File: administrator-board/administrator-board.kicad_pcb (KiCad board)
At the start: 2 copper layers, 24 parts, among them J2 Conn_01x06, J3 Conn_01x06, SW2 SW_Push, SW3 SW_Push, SW4 SW_Push, SW5 SW_Push

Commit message: 基盤PCB途中までいけた
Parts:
- moved REF** 3.91 mm to (154.0, 94.0)
- moved REF** 2.50 mm to (154.0, 129.0)
- moved R5 2.26 mm to (135.5, 111.8)
- moved REF** 2.00 mm to (87.0, 129.0)
- moved D5 1.88 mm to (135.5, 107.0)
- moved D4 1.88 mm to (121.5, 106.7)
- moved R4 1.85 mm to (121.6, 111.0)
- moved R8 1.36 mm to (128.3, 106.7)
- moved D3 1.28 mm to (110.1, 106.5)
- moved R3 1.28 mm to (110.1, 111.0)
- moved SW5 1.13 mm to (135.2, 97.1)
- moved REF** 1.12 mm to (87.0, 94.0)
- moved R7 0.66 mm to (115.9, 106.5)
- moved R9 0.35 mm to (142.2, 107.0)
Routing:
- net +3.3V: track 0.00 -> 86.4 mm
- net SW4: track 0.00 -> 38.1 mm
- net SW1: track 0.00 -> 35.8 mm
- net SW2: track 0.00 -> 35.6 mm
- net SW3: track 0.00 -> 33.3 mm
- net Net-(D1-K): track 0.00 -> 7.81 mm
- net Net-(D5-K): track 0.00 -> 4.76 mm
- net Net-(D3-K): track 0.00 -> 4.50 mm
- net Net-(D4-K): track 0.00 -> 4.32 mm
- net Net-(D2-K): track 0.00 -> 4.02 mm
- net GND: track 0.00 -> 0.18 mm, vias 0 -> 4
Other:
- board outline added: 75 x 43 mm

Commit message: PCB完成
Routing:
- net GND: vias 4 -> 27
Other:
- board text added: "Adminstrator Board"
- board text added: "SW1 3.3V SW2 GND"
- board text added: "SW3 3.3V SW4 GND"
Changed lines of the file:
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@@
 			(outputformat 1)
 			(mirror no)
-			(drillshape 1)
+			(drillshape 0)
 			(scaleselection 1)
-			(outputdirectory "")
+			(outputdirectory "admin-boardv1.0")
 		)
 	)
@@
 		(layer "Edge.Cuts")
 	)
+	(gr_text "Adminstrator Board"
+		(at 92.5 93 0)
+		(layer "F.SilkS")
+		(effects
+			(font
+				(size 1 1)
+				(thickness 0.1)
+			)
+			(justify left bottom)
+		)
+	)
+	(gr_text "SW1 3.3V SW2 GND"
+		(at 98.5 118.5 0)
+		(layer "F.SilkS")
+		(effects
+			(font
+				(size 1 1)
+				(thickness 0.1)
+			)
+			(justify left bottom)
+		)
+	)
+	(gr_text "SW3 3.3V SW4 GND"
+		(at 120.5 118 0)
+		(layer "F.SilkS")
+		(effects
+			(font
+				(size 1 1)
+				(thickness 0.1)
+			)
+			(justify left bottom)
+		)
+	)
 	(segment
 		(start 115.015 106.5)
@@
 	)
 	(via
-		(at 145 130)
+		(at 155 105)
+		(size 0.6)
+		(drill 0.3)
+		(layers "F.Cu" "B.Cu")
+		(free yes)
+		(net "GND")
+	)
+	(via
+		(at 125.5 105)
+		(size 0.6)
+		(drill 0.3)
+		(layers "F.Cu" "B.Cu")
+		(free yes)
+		(net "GND")
+	)
+	(via
+		(at 155 125)
+		(size 0.6)
+		(drill 0.3)
+		(layers "F.Cu" "B.Cu")
+		(free yes)
+		(net "GND")
+	)
+	(via
+		(at 139 104.5)
+		(size 0.6)
+		(drill 0.3)
+		(layers "F.Cu" "B.Cu")
+		(free yes)
+		(net "GND")
+	)
+	(via
+		(at 135 95)
+		(size 0.6)
+		(drill 0.3)
+		(layers "F.Cu" "B.Cu")
+		(free yes)
+		(net "GND")
+	)
+	(via
+		(at 150 130)
 		(size 0.6)
 		(drill 0.3)
@@
 	)
 	(via
-		(at 145 95)
+		(at 120 95)
+		(size 0.6)
+		(drill 0.3)
+		(layers "F.Cu" "B.Cu")
+		(free yes)
+		(net "GND")
+	)
+	(via
+		(at 85 105)
+		(size 0.6)
+		(drill 0.3)
+		(layers "F.Cu" "B.Cu")
+		(free yes)
+		(net "GND")
+	)
+	(via
+		(at 120 130)
+		(size 0.6)
+		(drill 0.3)
+		(layers "F.Cu" "B.Cu")
+		(free yes)
+		(net "GND")
+	)
+	(via
+		(at 111 109)
+		(size 0.6)
+		(drill 0.3)
+		(layers "F.Cu" "B.Cu")
+		(free yes)
+		(net "GND")
+	)
+	(via
+		(at 131.5 100)
+		(size 0.6)
+		(drill 0.3)
+		(layers "F.Cu" "B.Cu")
+		(free yes)
+		(net "GND")
+	)
+	(via
+		(at 99.5 108)
+		(size 0.6)
+		(drill 0.3)
+		(layers "F.Cu" "B.Cu")
+		(free yes)
+		(net "GND")
+	)
+	(via
+		(at 107 104)
+		(size 0.6)
+		(drill 0.3)
+		(layers "F.Cu" "B.Cu")
+		(free yes)
+		(net "GND")
+	)
+	(via
+		(at 126 120)
+		(size 0.6)
+		(drill 0.3)
+		(layers "F.Cu" "B.Cu")
+		(free yes)
+		(net "GND")
+	)
+	(via
+		(at 105 130)
+		(size 0.6)
+		(drill 0.3)
+		(layers "F.Cu" "B.Cu")
+		(free yes)
+		(net "GND")
+	)
+	(via
+		(at 121.5 109)
+		(size 0.6)
+		(drill 0.3)
+		(layers "F.Cu" "B.Cu")
+		(free yes)
+		(net "GND")
+	)
+	(via
+		(at 135 130)
+		(size 0.6)
+		(drill 0.3)
+		(layers "F.Cu" "B.Cu")
+		(free yes)
+		(net "GND")
+	)
+	(via
+		(at 150 95)
+		(size 0.6)
+		(drill 0.3)
+		(layers "F.Cu" "B.Cu")
+		(free yes)
+		(net "GND")
+	)
+	(via
+		(at 85 115)
+		(size 0.6)
+		(drill 0.3)
+		(layers "F.Cu" "B.Cu")
+		(free yes)
+		(net "GND")
+	)
+	(via
+		(at 155 115)
+		(size 0.6)
+		(drill 0.3)
+		(layers "F.Cu" "B.Cu")
+		(free yes)
+		(net "GND")
+	)
+	(via
+		(at 85 125)
+		(size 0.6)
+		(drill 0.3)
+		(layers "F.Cu" "B.Cu")
+		(free yes)
+		(net "GND")
+	)
+	(via
+		(at 136.5 109.5)
+		(size 0.6)
+		(drill 0.3)
+		(layers "F.Cu" "B.Cu")
+		(free yes)
+		(net "GND")
+	)
+	(via
+		(at 107 119.5)
+		(size 0.6)
+		(drill 0.3)
+		(layers "F.Cu" "B.Cu")
+		(free yes)
+		(net "GND")
+	)
+	(via
+		(at 113.5 104)
+		(size 0.6)
+		(drill 0.3)
+		(layers "F.Cu" "B.Cu")
+		(free yes)
+		(net "GND")
+	)
+	(via
+		(at 105 95)
 		(size 0.6)
 		(drill 0.3)
@@
 		(polygon
 			(pts
-				(xy 81.880753 88.92665) (xy 82.100783 138.537915) (xy 158.120288 138.200712) (xy 157.881038 88.573702)
+				(xy 82 88.92665) (xy 82.081403 134.168198) (xy 158.099222 133.831001) (xy 157.881038 88.573702)
 			)
 		)

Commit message: PCB完成
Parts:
- moved R5 2.01 mm to (136.5, 110.0)
- moved SW3 1.80 mm to (121.8, 95.8)
- moved J2 1.75 mm to (125.0, 123.0)
- moved R2 1.55 mm to (97.0, 110.0)
- moved D2 1.46 mm to (97.0, 106.0)
- moved SW1 1.46 mm to (94.8, 95.8)
- moved R4 1.37 mm to (122.5, 110.0)
- moved SW4 1.36 mm to (135.0, 95.8)
- moved SW2 1.25 mm to (108.5, 95.8)
- moved D5 1.12 mm to (136.5, 106.5)
- moved R3 1.00 mm to (110.1, 110.0)
- moved D4 0.99 mm to (122.5, 106.5)
- moved R8 0.93 mm to (129.2, 106.5)
- moved R6 0.77 mm to (102.0, 106.0)
- moved R9 0.52 mm to (142.4, 106.5)
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- renumbered SW2 to SW1, SW3 to SW2, SW4 to SW3, SW5 to SW4
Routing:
- net SW1: track 35.8 -> 32.7 mm
- net SW2: track 35.6 -> 38.1 mm
- net SW3: track 33.3 -> 34.8 mm
- net Net-(D5-K): track 4.76 -> 3.52 mm
- net +3.3V: track 86.4 -> 87.6 mm
- net SW4: track 38.1 -> 39.2 mm
- net Net-(D3-K): track 4.50 -> 3.52 mm
- net Net-(D1-K): track 7.81 -> 6.85 mm
- net Net-(D4-K): track 4.32 -> 3.52 mm
- net GND: vias 27 -> 29
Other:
- board text added: "designed by KamagataAkeru"

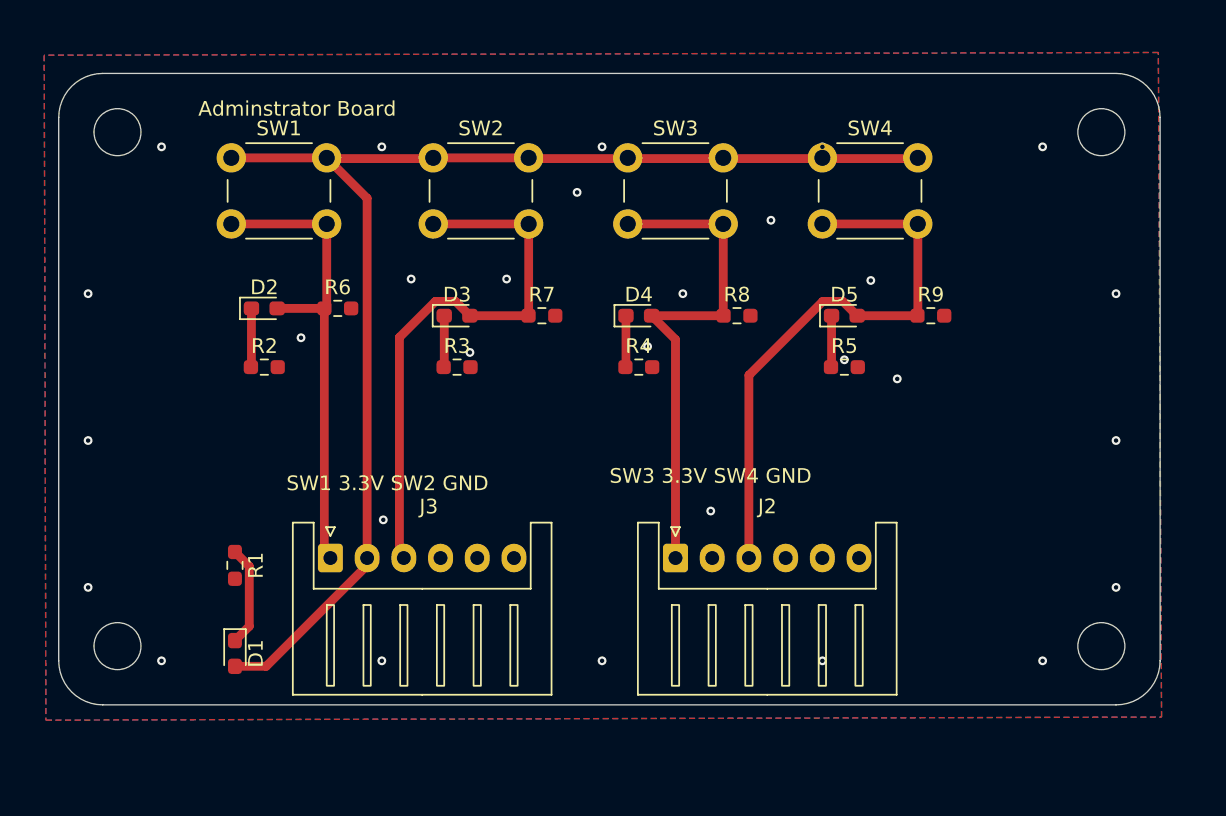
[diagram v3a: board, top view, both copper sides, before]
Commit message: fix:ビアの位置がずれていたので修正し未配線を解決、クリアランス設定をやってDLC
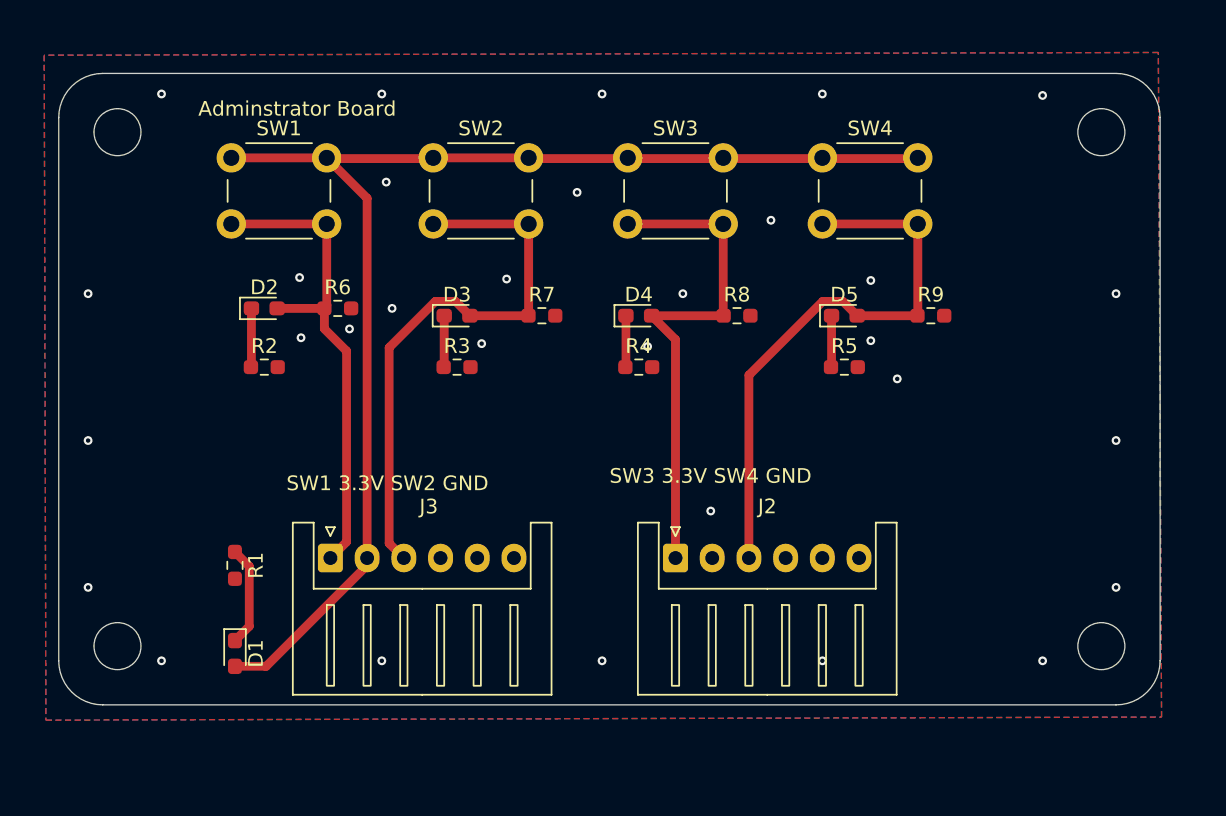
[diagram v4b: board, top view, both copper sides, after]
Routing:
- net SW1: track 32.7 -> 33.6 mm
- net SW2: track 38.1 -> 38.7 mm
- net GND: vias 29 -> 31
